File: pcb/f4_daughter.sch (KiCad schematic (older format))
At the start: 0 parts

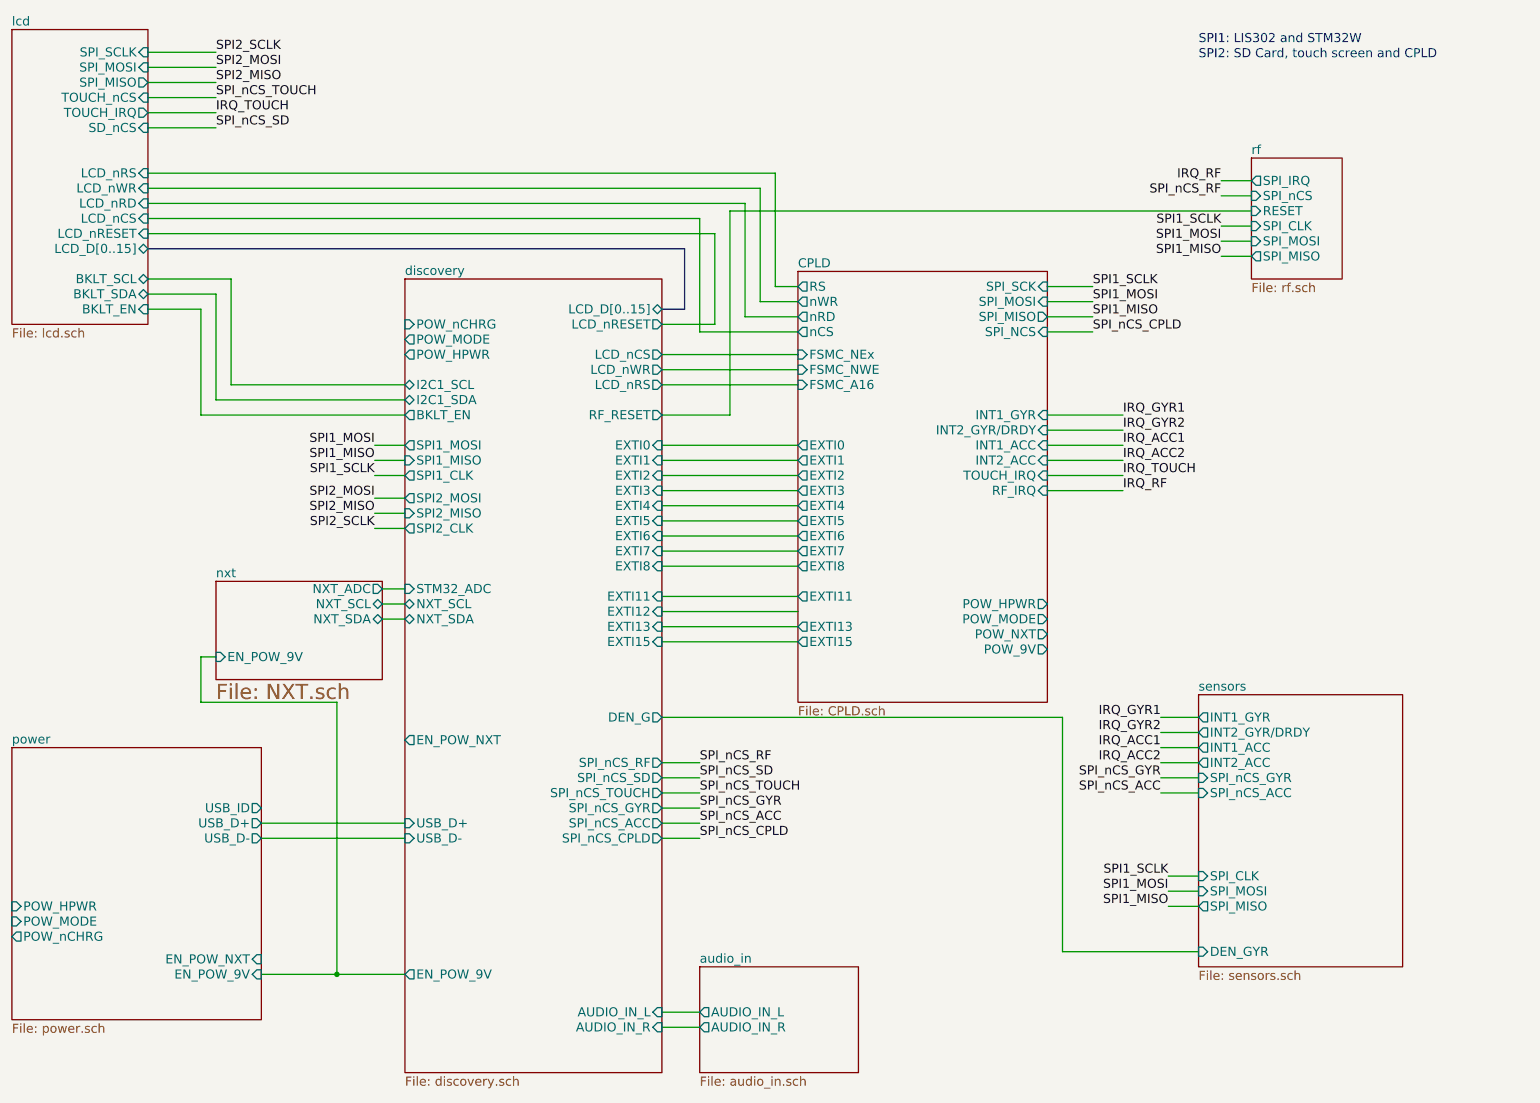
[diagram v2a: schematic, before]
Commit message: Modified labels on discover.sch and rearranged sheet disposition in the top-level schematic.
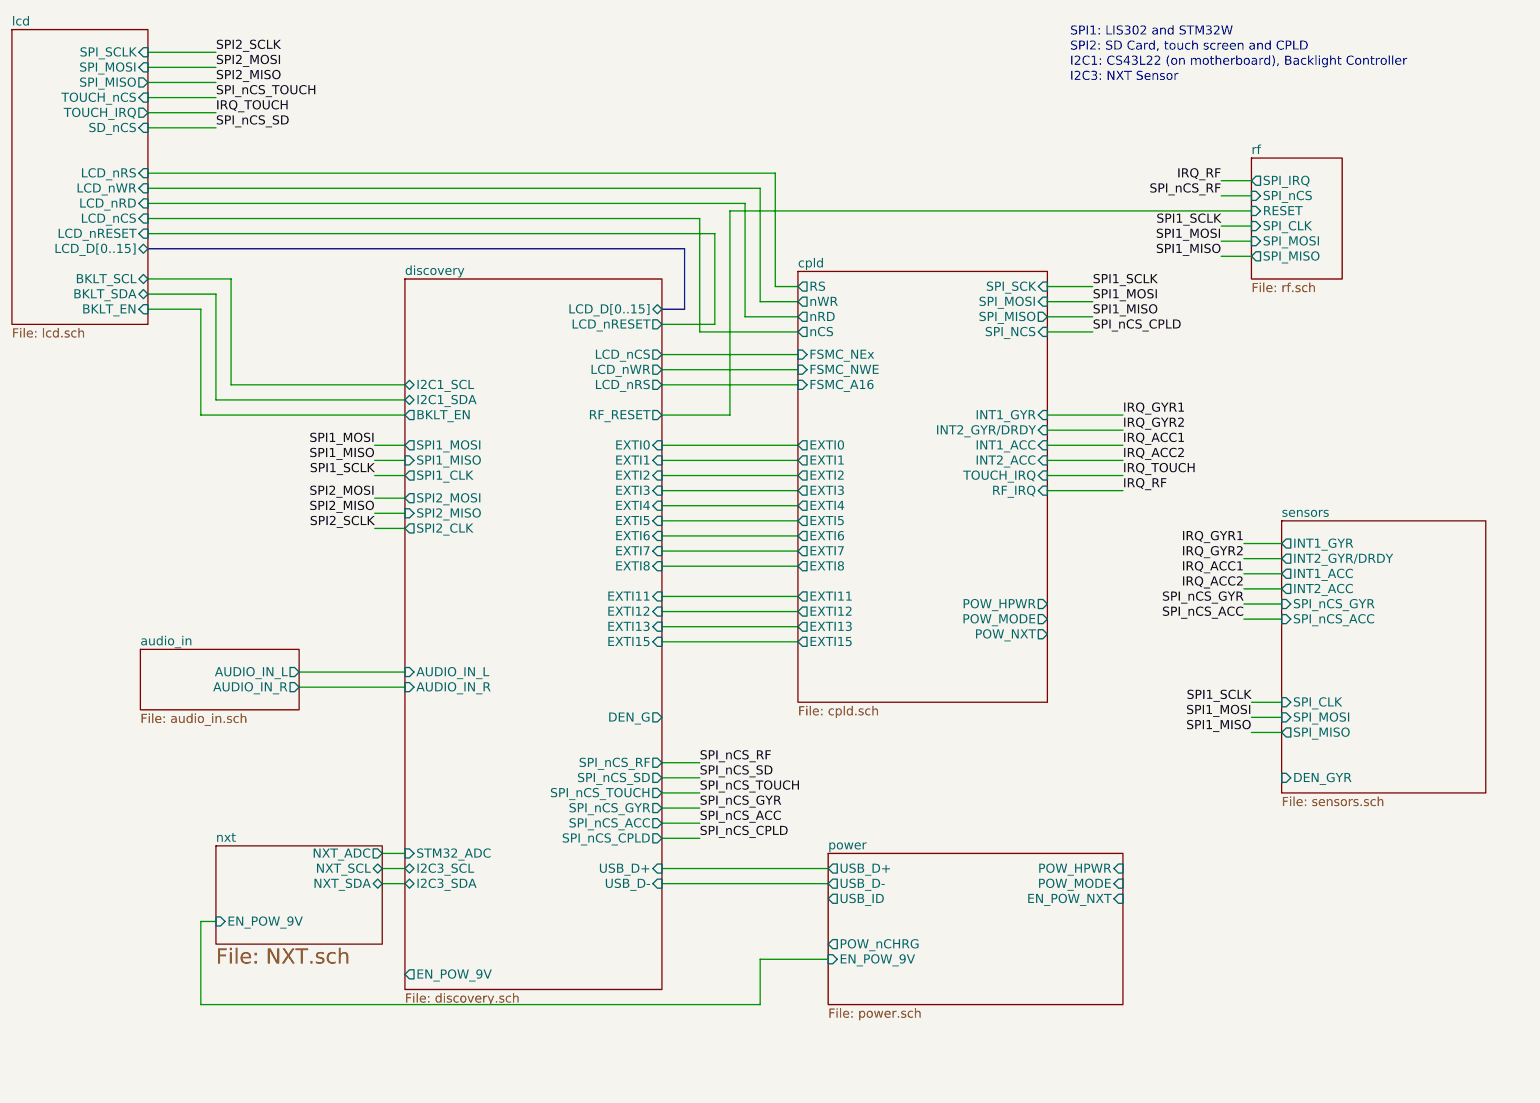
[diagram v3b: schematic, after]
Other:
- note added: "I2C1: CS43L22 (on motherboard), Backlight Controller"
- note added: "I2C3: NXT Sensor"

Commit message: Forgot to commit the actual changed files two commits ago.
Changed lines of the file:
@@
-EESchema Schematic File Version 2  date 12/30/2012 6:01:05 PM
+EESchema Schematic File Version 2  date 12/30/2012 6:18:52 PM
 LIBS:power
 LIBS:device
@@
 Comment4 ""
 $EndDescr
-$Sheet
-S 9750 3900 1350 1800
-U 50C1133E
-F0 "sensors" 60
-F1 "sensors.sch" 60
-F2 "INT2_GYR/DRDY" O L 9750 4150 60
-F3 "INT1_GYR" O L 9750 4050 60
-F4 "INT2_ACC" O L 9750 4350 60
-F5 "INT1_ACC" O L 9750 4250 60
-F6 "SPI_nCS_GYR" I L 9750 4450 60
-F7 "SPI_nCS_ACC" I L 9750 4550 60
-F8 "SPI_CLK" I L 9750 5100 60
-F9 "SPI_MOSI" I L 9750 5200 60
-F10 "SPI_MISO" O L 9750 5300 60
-F11 "DEN_GYR" I L 9750 5600 60
-$EndSheet
-Text Notes 8350 1000 0    60   ~ 0
-I2C3: NXT Sensor
-Text Notes 8350 900  0    60   ~ 0
-I2C1: CS43L22 (on motherboard), Backlight Controller
+Connection ~ 3800 7100
+Wire Wire Line
+	3800 7100 3800 6900
+Wire Wire Line
+	3800 6900 3950 6900
+Wire Wire Line
+	9700 5400 5650 5400
+Wire Wire Line
+	8200 4900 8400 4900
+Wire Wire Line
+	8400 4900 8400 6300
+Wire Wire Line
+	8400 6300 8200 6300
 Wire Wire Line
 	6300 7100 6300 6800
@@
 	8700 3400 8200 3400
 Wire Wire Line
-	9750 4150 9500 4150
+	9700 4150 9450 4150
 Wire Wire Line
 	9550 1650 9350 1650
@@
 	6100 3200 5650 3200
 Wire Wire Line
-	9750 4450 9500 4450
+	9700 4450 9450 4450
 Wire Wire Line
 	5650 5700 5900 5700
@@
 	3950 3400 3750 3400
 Wire Wire Line
-	9750 5200 9550 5200
+	9700 5200 9500 5200
 Wire Wire Line
 	2700 800  2250 800
@@
 	2700 900  2250 900
 Wire Wire Line
-	9750 5100 9550 5100
-Wire Wire Line
-	9750 5300 9550 5300
+	9700 5100 9500 5100
+Wire Wire Line
+	9700 5300 9500 5300
 Wire Wire Line
 	9550 2150 9350 2150
@@
 	9550 1750 9350 1750
 Wire Wire Line
-	9750 4550 9500 4550
+	9700 4550 9450 4550
 Wire Wire Line
 	6000 2600 5650 2600
@@
 	2250 1200 2700 1200
 Wire Wire Line
-	9750 4050 9500 4050
-Wire Wire Line
-	9750 4250 9500 4250
-Wire Wire Line
-	9750 4350 9500 4350
+	9700 4050 9450 4050
+Wire Wire Line
+	9700 4250 9450 4250
+Wire Wire Line
+	9700 4350 9450 4350
 Wire Wire Line
 	8700 3500 8200 3500
@@
 Wire Wire Line
 	6300 6800 6750 6800
+Wire Wire Line
+	8200 5000 8300 5000
+Wire Wire Line
+	8300 5000 8300 6200
+Wire Wire Line
+	8300 6200 8200 6200
+Wire Wire Line
+	8200 6400 8500 6400
+Wire Wire Line
+	8500 6400 8500 4800
+Wire Wire Line
+	8500 4800 8200 4800
+Wire Wire Line
+	5650 6700 6750 6700
+$Sheet
+S 9700 3900 1350 1800
+U 50C1133E
+F0 "sensors" 60
+F1 "sensors.sch" 60
+F2 "INT2_GYR/DRDY" O L 9700 4150 60
+F3 "INT1_GYR" O L 9700 4050 60
+F4 "INT2_ACC" O L 9700 4350 60
+F5 "INT1_ACC" O L 9700 4250 60
+F6 "SPI_nCS_GYR" I L 9700 4450 60
+F7 "SPI_nCS_ACC" I L 9700 4550 60
+F8 "SPI_CLK" I L 9700 5100 60
+F9 "SPI_MOSI" I L 9700 5200 60
+F10 "SPI_MISO" O L 9700 5300 60
+F11 "DEN_GYR" I L 9700 5400 60
+$EndSheet
+Text Notes 8350 1000 0    60   ~ 0
+I2C3: NXT Sensor
+Text Notes 8350 900  0    60   ~ 0
+I2C1: CS43L22 (on motherboard), Backlight Controller
 $Sheet
 S 3950 2300 1700 4700
@@
 F24 "LCD_nRS" O R 5650 3000 60
 F25 "SPI_nCS_SD" O R 5650 5600 60
-F26 "DEN_G" O R 5650 5200 60
+F26 "DEN_G" O R 5650 5400 60
 F27 "SPI2_MISO" I L 3950 3850 60
 F28 "SPI1_CLK" O L 3950 3600 60
@@
 F43 "I2C1_SCL" B L 3950 3000 60
 F44 "I2C1_SDA" B L 3950 3100 60
+F45 "POW_nCHRG" I R 5650 6700 60
 $EndSheet
 Text Label 8500 2650 0    60   ~ 0
@@
 Text Label 8700 3500 0    60   ~ 0
 IRQ_ACC2
-Text Label 9500 4350 2    60   ~ 0
+Text Label 9450 4350 2    60   ~ 0
 IRQ_ACC2
-Text Label 9500 4250 2    60   ~ 0
+Text Label 9450 4250 2    60   ~ 0
 IRQ_ACC1
-Text Label 9500 4150 2    60   ~ 0
+Text Label 9450 4150 2    60   ~ 0
 IRQ_GYR2
-Text Label 9500 4050 2    60   ~ 0
+Text Label 9450 4050 2    60   ~ 0
 IRQ_GYR1
 Text Label 9350 1650 2    60   ~ 0
@@
 Text Label 2700 1200 0    60   ~ 0
 IRQ_TOUCH
-Text Label 9500 4550 2    60   ~ 0
+Text Label 9450 4550 2    60   ~ 0
 SPI_nCS_ACC
-Text Label 9500 4450 2    60   ~ 0
+Text Label 9450 4450 2    60   ~ 0
 SPI_nCS_GYR
 $Sheet
@@
 F0 "cpld" 60
 F1 "cpld.sch" 60
-F2 "POW_HPWR" O R 8200 4450 60
-F3 "POW_NXT" O R 8200 4650 60
-F4 "POW_MODE" O R 8200 4550 60
+F2 "POW_HPWR" O R 8200 4800 60
+F3 "POW_NXT" O R 8200 5000 60
+F4 "POW_MODE" O R 8200 4900 60
 F5 "FSMC_A16" I L 6550 3000 60
 F6 "FSMC_NWE" I L 6550 2900 60
@@
 Text Label 9350 2150 2    60   ~ 0
 SPI1_MISO
-Text Label 9550 5300 2    60   ~ 0
+Text Label 9500 5300 2    60   ~ 0
 SPI1_MISO
-Text Label 9550 5200 2    60   ~ 0
+Text Label 9500 5200 2    60   ~ 0
 SPI1_MOSI
-Text Label 9550 5100 2    60   ~ 0
+Text Label 9500 5100 2    60   ~ 0
 SPI1_SCLK
 Text Label 2700 1000 0    60   ~ 0
@@
 $EndSheet
 $Sheet
-S 6750 6100 1950 1000
+S 6750 6100 1450 1000
 U 500B69F1
 F0 "power" 60
@@
 F3 "USB_D+" O L 6750 6200 60
 F4 "USB_D-" O L 6750 6300 60
-F5 "POW_MODE" I R 8700 6300 60
+F5 "POW_MODE" I R 8200 6300 60
 F6 "POW_nCHRG" O L 6750 6700 60
-F7 "POW_HPWR" I R 8700 6200 60
-F8 "EN_POW_NXT" I R 8700 6400 60
+F7 "POW_HPWR" I R 8200 6400 60
+F8 "EN_POW_NXT" I R 8200 6200 60
 F9 "EN_POW_9V" I L 6750 6800 60
 $EndSheet

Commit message: cpld: Added two LEDS and removed the EXTIO0 and EXTI1 since they are already used by the sensor discovery: Rearranged pins to connect both audio lines to adjacent ADCs as well as to free up pins as a result of not using EXTI0 and EXTI1 f4_daughter: Moved around some stuff and changed relevant text
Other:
- note added: "SPI1: LSM330 and STM32W"
- note removed: "SPI1: LIS302 and STM32W"
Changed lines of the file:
@@
-EESchema Schematic File Version 2  date 12/30/2012 6:18:52 PM
+EESchema Schematic File Version 2  date 1/3/2013 4:23:52 PM
 LIBS:power
 LIBS:device
@@
 Sheet 1 9
 Title ""
-Date "30 dec 2012"
+Date "3 jan 2013"
 Rev ""
 Comp ""
@@
 Comment4 ""
 $EndDescr
-Connection ~ 3800 7100
-Wire Wire Line
-	3800 7100 3800 6900
-Wire Wire Line
-	3800 6900 3950 6900
-Wire Wire Line
-	9700 5400 5650 5400
-Wire Wire Line
-	8200 4900 8400 4900
-Wire Wire Line
-	8400 4900 8400 6300
-Wire Wire Line
-	8400 6300 8200 6300
-Wire Wire Line
-	6300 7100 6300 6800
-Wire Wire Line
-	6300 7100 2600 7100
-Wire Wire Line
-	2600 7100 2600 6550
-Wire Wire Line
-	6750 6300 5650 6300
-Wire Wire Line
-	2250 2500 2600 2500
-Wire Wire Line
-	2600 2500 2600 3200
-Wire Wire Line
-	2600 3200 3950 3200
-Wire Wire Line
-	2250 2300 2800 2300
-Wire Wire Line
-	2800 2300 2800 3000
-Wire Wire Line
-	2800 3000 3950 3000
-Wire Wire Line
-	6550 4600 5650 4600
-Wire Wire Line
-	6550 4400 5650 4400
-Wire Wire Line
-	5650 6000 5900 6000
-Wire Wire Line
-	5900 5900 5650 5900
-Wire Wire Line
-	9550 1850 6100 1850
-Wire Wire Line
-	6100 1850 6100 3200
-Wire Wire Line
-	8700 3700 8200 3700
-Wire Wire Line
-	2250 1900 5900 1900
-Wire Wire Line
-	5900 1900 5900 2650
-Wire Wire Line
-	5900 2650 6550 2650
-Wire Wire Line
-	2250 1700 6300 1700
-Wire Wire Line
-	6300 1700 6300 2450
-Wire Wire Line
-	6300 2450 6550 2450
-Wire Wire Line
-	5650 2800 6550 2800
-Wire Wire Line
-	8700 3200 8200 3200
-Wire Wire Line
-	8700 3400 8200 3400
-Wire Wire Line
-	9700 4150 9450 4150
-Wire Wire Line
-	9550 1650 9350 1650
-Wire Wire Line
-	5650 4100 6550 4100
-Wire Wire Line
-	5650 3900 6550 3900
-Wire Wire Line
-	5650 3700 6550 3700
-Wire Wire Line
-	5650 3500 6550 3500
-Wire Wire Line
-	5650 3000 6550 3000
-Wire Wire Line
-	6100 3200 5650 3200
-Wire Wire Line
-	9700 4450 9450 4450
-Wire Wire Line
-	5650 5700 5900 5700
-Wire Wire Line
-	5650 5500 5900 5500
-Wire Wire Line
-	2250 1100 2700 1100
-Wire Wire Line
-	3950 6100 3800 6100
-Wire Wire Line
-	3950 6200 3800 6200
-Wire Wire Line
-	8200 2550 8500 2550
-Wire Wire Line
-	8500 2350 8200 2350
-Wire Wire Line
-	3950 3850 3750 3850
-Wire Wire Line
-	3950 3600 3750 3600
-Wire Wire Line
-	3950 3400 3750 3400
-Wire Wire Line
-	9700 5200 9500 5200
-Wire Wire Line
-	2700 800  2250 800
-Wire Wire Line
-	2700 1000 2250 1000
+Wire Wire Line
+	5650 6700 6750 6700
+Wire Wire Line
+	8200 4800 8500 4800
+Wire Wire Line
+	8500 4800 8500 6400
+Wire Wire Line
+	8500 6400 8200 6400
+Wire Wire Line
+	8200 6200 8300 6200
+Wire Wire Line
+	8300 6200 8300 5000
+Wire Wire Line
+	8300 5000 8200 5000
+Wire Wire Line
+	6750 6800 6300 6800
+Wire Wire Line
+	3950 5000 3250 5000
+Wire Wire Line
+	3250 4900 3950 4900
+Wire Wire Line
+	5650 6200 6750 6200
+Wire Wire Line
+	3950 3100 2700 3100
+Wire Wire Line
+	2700 3100 2700 2400
+Wire Wire Line
+	2700 2400 2250 2400
+Wire Wire Line
+	6550 4700 5650 4700
+Wire Wire Line
+	5650 4500 6550 4500
+Wire Wire Line
+	2700 6550 2600 6550
+Wire Bus Line
+	5650 2500 5800 2500
+Wire Wire Line
+	5900 5800 5650 5800
+Wire Wire Line
+	2250 1800 6200 1800
+Wire Wire Line
+	6200 1800 6200 2550
+Wire Wire Line
+	8700 3600 8200 3600
+Wire Wire Line
+	6200 2550 6550 2550
+Wire Wire Line
+	2250 1600 6400 1600
+Wire Wire Line
+	6400 1600 6400 2350
+Wire Wire Line
+	6400 2350 6550 2350
+Wire Wire Line
+	8700 3300 8200 3300
+Wire Wire Line
+	8700 3500 8200 3500
+Wire Wire Line
+	9700 4350 9450 4350
+Wire Wire Line
+	9700 4250 9450 4250
+Wire Wire Line
+	9700 4050 9450 4050
+Wire Wire Line
+	2250 1200 2700 1200
+Wire Wire Line
+	5650 4200 6550 4200
+Wire Wire Line
+	5650 4000 6550 4000
+Wire Wire Line
+	5650 3800 6550 3800
+Wire Wire Line
+	5650 3600 6550 3600
+Wire Wire Line
+	5650 3400 6550 3400
+Wire Wire Line
+	5650 2900 6550 2900
+Wire Wire Line
+	5650 2600 6000 2600
+Wire Wire Line
+	9700 4550 9450 4550
+Wire Wire Line
+	9550 1750 9350 1750
+Wire Wire Line
+	5650 5600 5900 5600
+Wire Wire Line
+	2250 1300 2700 1300
+Wire Wire Line
+	3950 6300 3800 6300
+Wire Wire Line
+	8200 2650 8500 2650
+Wire Wire Line
+	8200 2450 8500 2450
+Wire Wire Line
+	3950 3950 3750 3950
+Wire Wire Line
+	3950 3750 3750 3750
+Wire Wire Line
+	3950 3500 3750 3500
+Wire Wire Line
+	9550 2050 9350 2050
+Wire Wire Line
+	9550 1950 9350 1950
+Wire Wire Line
+	9550 2150 9350 2150
+Wire Wire Line
+	9700 5300 9500 5300
+Wire Wire Line
+	9700 5100 9500 5100
+Wire Wire Line
+	2700 900  2250 900
+Wire Wire Line
+	2250 2000 6000 2000
+Wire Wire Line
+	6000 2000 6000 2600
+Wire Bus Line
+	2250 2100 5800 2100
 Wire Bus Line
 	5800 2100 5800 2500
-Wire Bus Line
-	5800 2100 2250 2100
-Wire Wire Line
-	6000 2000 6000 2600
-Wire Wire Line
-	6000 2000 2250 2000
-Wire Wire Line
-	2700 900  2250 900
-Wire Wire Line
-	9700 5100 9500 5100
-Wire Wire Line
-	9700 5300 9500 5300
-Wire Wire Line
-	9550 2150 9350 2150
-Wire Wire Line
-	9550 1950 9350 1950
-Wire Wire Line
-	9550 2050 9350 2050
-Wire Wire Line
-	3950 3500 3750 3500
-Wire Wire Line
-	3950 3750 3750 3750
-Wire Wire Line
-	3950 3950 3750 3950
-Wire Wire Line
-	8200 2450 8500 2450
-Wire Wire Line
-	8200 2650 8500 2650
-Wire Wire Line
-	3950 6300 3800 6300
-Wire Wire Line
-	2250 1300 2700 1300
-Wire Wire Line
-	5650 5600 5900 5600
-Wire Wire Line
-	9550 1750 9350 1750
-Wire Wire Line
-	9700 4550 9450 4550
-Wire Wire Line
-	6000 2600 5650 2600
-Wire Wire Line
-	5650 2900 6550 2900
-Wire Wire Line
-	5650 3400 6550 3400
-Wire Wire Line
-	5650 3600 6550 3600
-Wire Wire Line
-	5650 3800 6550 3800
-Wire Wire Line
-	5650 4000 6550 4000
-Wire Wire Line
-	5650 4200 6550 4200
-Wire Wire Line
-	2250 1200 2700 1200
-Wire Wire Line
-	9700 4050 9450 4050
-Wire Wire Line
-	9700 4250 9450 4250
-Wire Wire Line
-	9700 4350 9450 4350
-Wire Wire Line
-	8700 3500 8200 3500
-Wire Wire Line
-	8700 3300 8200 3300
-Wire Wire Line
-	6550 2350 6400 2350
-Wire Wire Line
-	6400 2350 6400 1600
-Wire Wire Line
-	6400 1600 2250 1600
-Wire Wire Line
-	6550 2550 6200 2550
-Wire Wire Line
-	8700 3600 8200 3600
-Wire Wire Line
-	6200 2550 6200 1800
-Wire Wire Line
-	6200 1800 2250 1800
-Wire Wire Line
-	5900 5800 5650 5800
-Wire Bus Line
-	5800 2500 5650 2500
-Wire Wire Line
-	2600 6550 2700 6550
-Wire Wire Line
-	5650 4500 6550 4500
-Wire Wire Line
-	6550 4700 5650 4700
-Wire Wire Line
-	2250 2400 2700 2400
-Wire Wire Line
-	2700 2400 2700 3100
-Wire Wire Line
-	2700 3100 3950 3100
-Wire Wire Line
-	5650 6200 6750 6200
-Wire Wire Line
-	3250 4900 3950 4900
-Wire Wire Line
-	3950 5000 3250 5000
-Wire Wire Line
-	6300 6800 6750 6800
-Wire Wire Line
-	8200 5000 8300 5000
-Wire Wire Line
-	8300 5000 8300 6200
-Wire Wire Line
-	8300 6200 8200 6200
-Wire Wire Line
-	8200 6400 8500 6400
-Wire Wire Line
-	8500 6400 8500 4800
-Wire Wire Line
-	8500 4800 8200 4800
-Wire Wire Line
-	5650 6700 6750 6700
+Wire Wire Line
+	2700 1000 2250 1000
+Wire Wire Line
+	2700 800  2250 800
+Wire Wire Line
+	9700 5200 9500 5200
+Wire Wire Line
+	3950 3400 3750 3400
+Wire Wire Line
+	3950 3600 3750 3600
+Wire Wire Line
+	3950 3850 3750 3850
+Wire Wire Line
+	8500 2350 8200 2350
+Wire Wire Line
+	8200 2550 8500 2550
+Wire Wire Line
+	3950 6200 3800 6200
+Wire Wire Line
+	3950 6100 3800 6100
+Wire Wire Line
+	2250 1100 2700 1100
+Wire Wire Line
+	5650 5500 5900 5500
+Wire Wire Line
+	5650 5700 5900 5700
+Wire Wire Line
+	9700 4450 9450 4450
+Wire Wire Line
+	5650 3200 6100 3200
+Wire Wire Line
+	5650 3000 6550 3000
+Wire Wire Line
+	5650 3500 6550 3500
+Wire Wire Line
+	5650 3700 6550 3700
+Wire Wire Line
+	5650 3900 6550 3900
+Wire Wire Line
+	5650 4100 6550 4100
+Wire Wire Line
+	9550 1650 9350 1650
+Wire Wire Line
+	9700 4150 9450 4150
+Wire Wire Line
+	8700 3400 8200 3400
+Wire Wire Line
+	8700 3200 8200 3200
+Wire Wire Line
+	5650 2800 6550 2800
+Wire Wire Line
+	6550 2450 6300 2450
+Wire Wire Line
+	6300 2450 6300 1700
+Wire Wire Line
+	6300 1700 2250 1700
+Wire Wire Line
+	6550 2650 5900 2650
+Wire Wire Line
+	5900 2650 5900 1900
+Wire Wire Line
+	5900 1900 2250 1900
+Wire Wire Line
+	8700 3700 8200 3700
+Wire Wire Line
+	6100 3200 6100 1850
+Wire Wire Line
+	6100 1850 9550 1850
+Wire Wire Line
+	5900 5900 5650 5900
+Wire Wire Line
+	5650 6000 5900 6000
+Wire Wire Line
+	6550 4400 5650 4400
+Wire Wire Line
+	6550 4600 5650 4600
+Wire Wire Line
+	3950 3000 2800 3000
+Wire Wire Line
+	2800 3000 2800 2300
+Wire Wire Line
+	2800 2300 2250 2300
+Wire Wire Line
+	3950 3200 2600 3200
+Wire Wire Line
+	2600 3200 2600 2500
+Wire Wire Line
+	2600 2500 2250 2500
+Wire Wire Line
+	6750 6300 5650 6300
+Wire Wire Line
+	2600 6550 2600 7100
+Wire Wire Line
+	2600 7100 6300 7100
+Wire Wire Line
+	6300 7100 6300 6800
+Wire Wire Line
+	8200 6300 8400 6300
+Wire Wire Line
+	8400 6300 8400 4900
+Wire Wire Line
+	8400 4900 8200 4900
+Wire Wire Line
+	9700 5400 5650 5400
+Wire Wire Line
+	3950 6900 3800 6900
+Wire Wire Line
+	3800 6900 3800 7100
+Connection ~ 3800 7100
 $Sheet
 S 9700 3900 1350 1800
@@
 SPI2: SD Card, touch screen and CPLD
 Text Notes 8350 700  0    60   ~ 0
-SPI1: LIS302 and STM32W
+SPI1: LSM330 and STM32W
 Text Label 2700 800  0    60   ~ 0
 SPI2_SCLK
